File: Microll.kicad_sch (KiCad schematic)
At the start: 5 parts

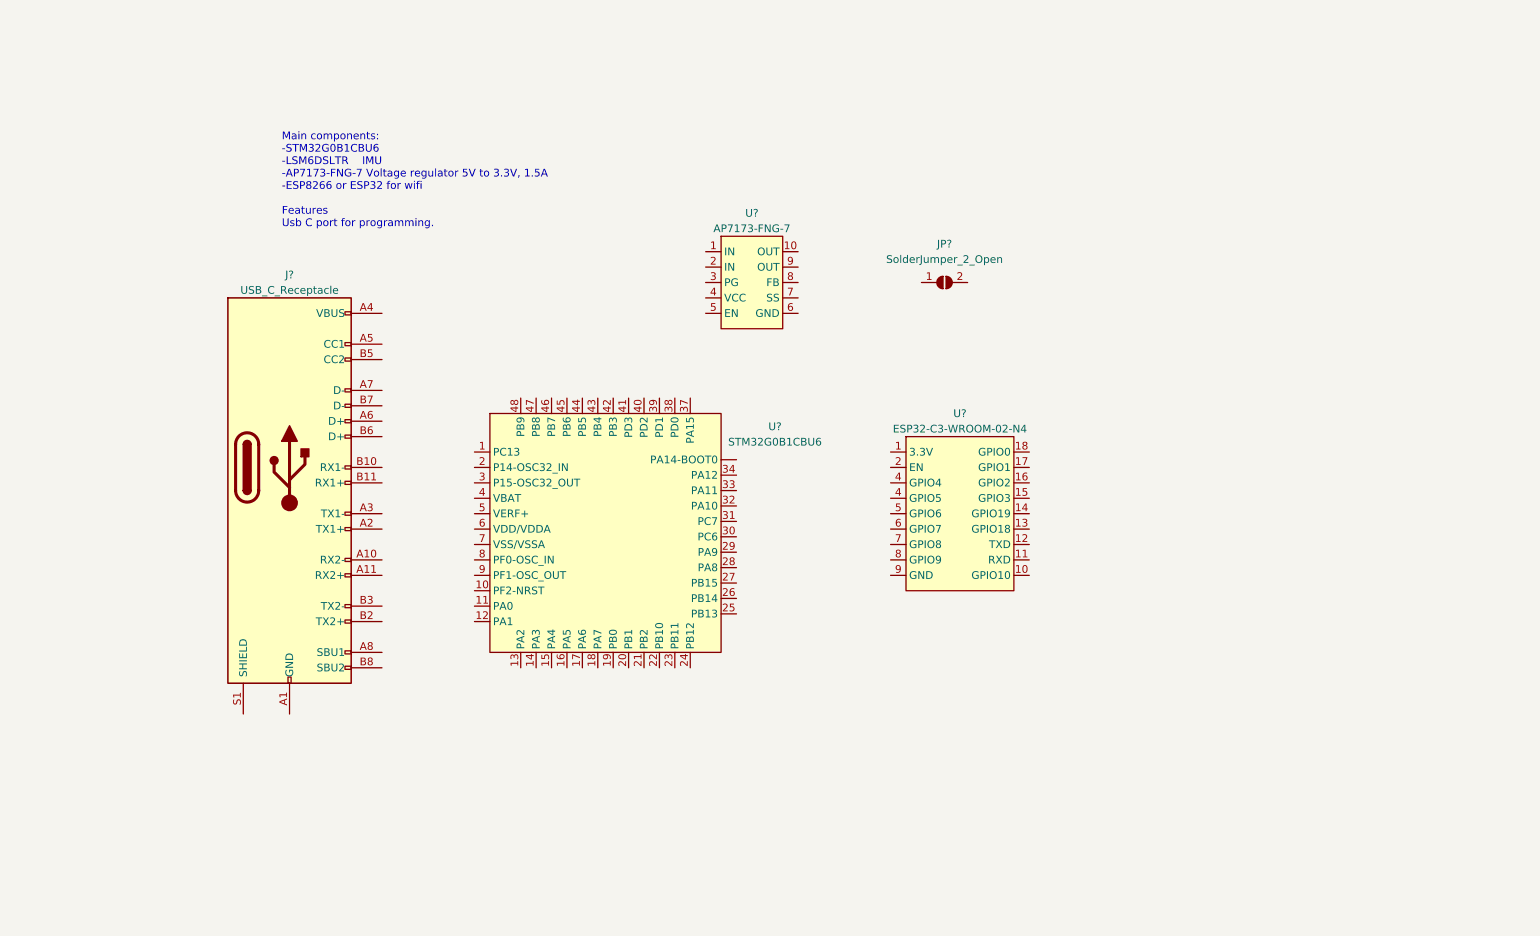
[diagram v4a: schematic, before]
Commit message: Added IMU. Initial placement of components on PCB to check spacing
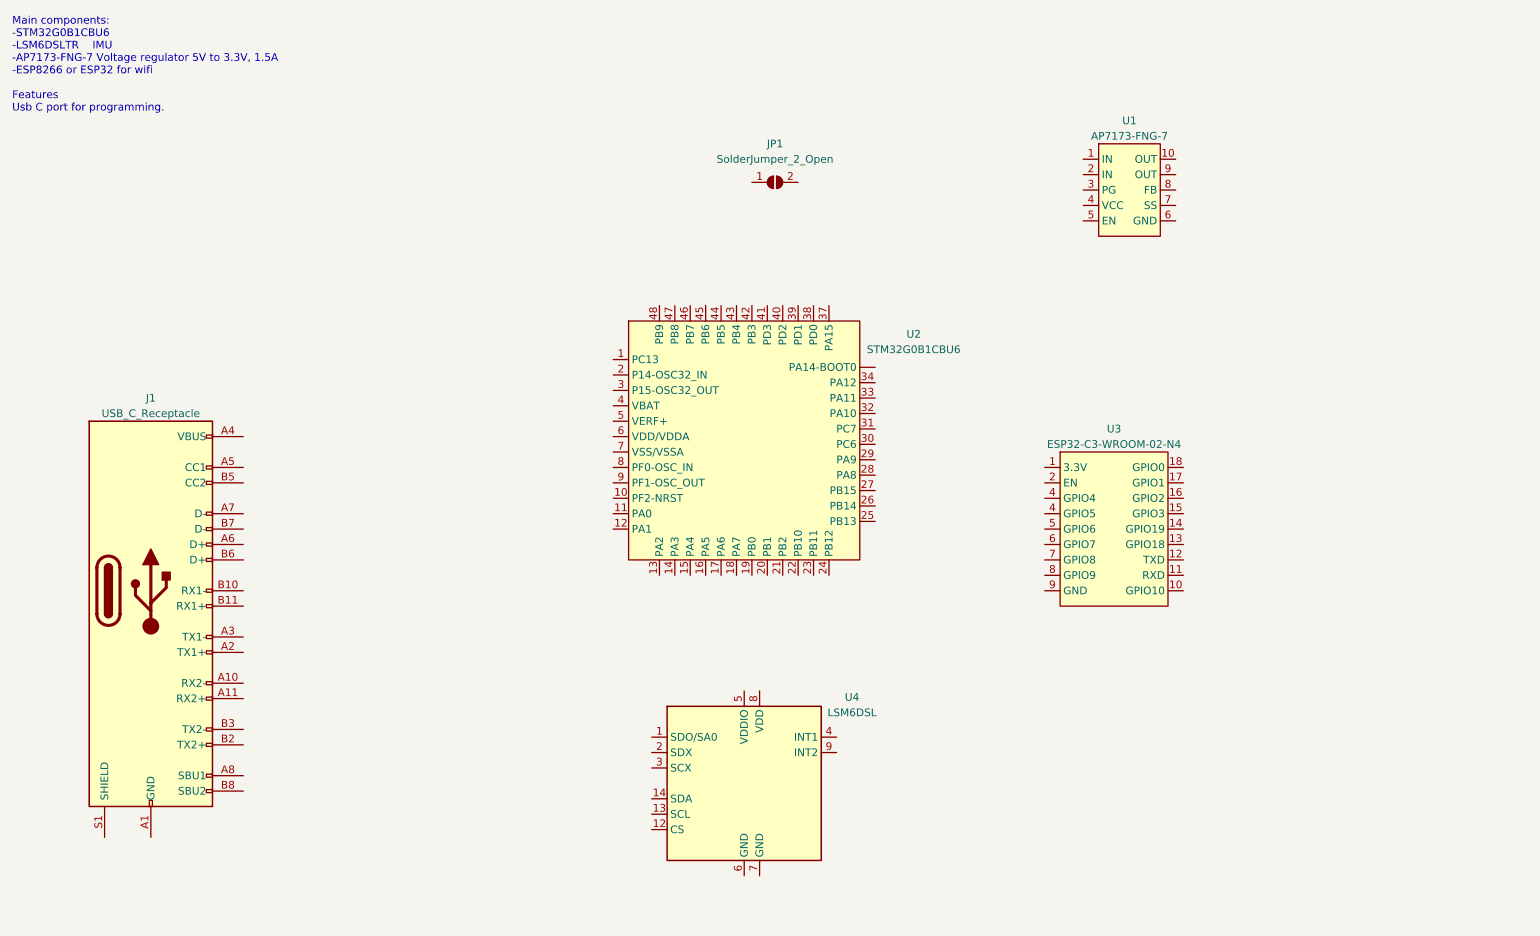
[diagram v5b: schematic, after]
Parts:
- added U4: LSM6DSL, Package_LGA:LGA-14_3x2.5mm_P0.5mm_LayoutBorder3x4y, symbol Sensor_Motion:LSM6DSL
- J1: renamed from J?; footprint (none) -> Connector_USB:USB_C_Receptacle_GCT_USB4105-xx-A_16P_TopMnt_Horizontal
- JP1: renamed from JP?; footprint (none) -> SolderJumper-2_P1.3mm_Open_RoundedPad1.0x1.5mm
- gave numbers to parts that had none: 3
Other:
- moved on the sheet: J1, JP1, U1, U2, U3
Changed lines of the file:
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@@
   (paper "A4")
   (text "Main components:\n-STM32G0B1CBU6	\n-LSM6DSLTR	IMU\n-AP7173-FNG-7 Voltage regulator 5V to 3.3V, 1.5A\n-ESP8266 or ESP32 for wifi\n\nFeatures\nUsb C port for programming."
-    (at 59.69 50.8 0)
+    (at 15.24 31.75 0)
     (effects (font (size 1.27 1.27)) (justify left bottom))
   )
-  (symbol (lib_id "Jumper:SolderJumper_2_Open") (at 168.91 59.69 0) (unit 1)
+  (symbol (lib_id "Jumper:SolderJumper_2_Open") (at 140.97 43.18 0) (unit 1)
     (in_bom yes) (on_board yes) (fields_autoplaced)
-    (property "Reference" "JP?" (id 0) (at 168.91 53.34 0))
-    (property "Value" "SolderJumper_2_Open" (id 1) (at 168.91 55.88 0))
-    (property "Footprint" "" (id 2) (at 168.91 59.69 0)
-      (effects (font (size 1.27 1.27)) hide)
-    )
-    (property "Datasheet" "~" (id 3) (at 168.91 59.69 0)
-      (effects (font (size 1.27 1.27)) hide)
-    )
-    (pin "1")
-    (pin "2")
-  )
-  (symbol (lib_id "ESP32:ESP32-C3-WROOM-02-N4") (at 171.45 93.98 0) (unit 1)
+    (property "Reference" "JP1" (id 0) (at 140.97 36.83 0))
+    (property "Value" "SolderJumper_2_Open" (id 1) (at 140.97 39.37 0))
+    (property "Footprint" "SolderJumper-2_P1.3mm_Open_RoundedPad1.0x1.5mm" (id 2) (at 140.97 43.18 0)
+      (effects (font (size 1.27 1.27)) hide)
+    )
+    (property "Datasheet" "~" (id 3) (at 140.97 43.18 0)
+      (effects (font (size 1.27 1.27)) hide)
+    )
+    (pin "1")
+    (pin "2")
+  )
+  (symbol (lib_id "ESP32:ESP32-C3-WROOM-02-N4") (at 196.85 96.52 0) (unit 1)
     (in_bom yes) (on_board yes)
-    (property "Reference" "U?" (id 0) (at 171.45 81.28 0))
-    (property "Value" "ESP32-C3-WROOM-02-N4" (id 1) (at 171.45 83.82 0))
-    (property "Footprint" "ESP32:ESP32-C3-WROOM-02-N4" (id 2) (at 171.45 93.98 0)
-      (effects (font (size 1.27 1.27)) hide)
-    )
-    (property "Datasheet" "" (id 3) (at 171.45 93.98 0)
+    (property "Reference" "U3" (id 0) (at 196.85 83.82 0))
+    (property "Value" "ESP32-C3-WROOM-02-N4" (id 1) (at 196.85 86.36 0))
+    (property "Footprint" "ESP32:ESP32-C3-WROOM-02-N4" (id 2) (at 196.85 96.52 0)
+      (effects (font (size 1.27 1.27)) hide)
+    )
+    (property "Datasheet" "" (id 3) (at 196.85 96.52 0)
       (effects (font (size 1.27 1.27)) hide)
     )
@@
     (pin "9")
   )
-  (symbol (lib_id "STM32:STM32G0B1CBU6") (at 113.03 101.6 0) (unit 1)
+  (symbol (lib_id "STM32:STM32G0B1CBU6") (at 135.89 86.36 0) (unit 1)
     (in_bom yes) (on_board yes) (fields_autoplaced)
-    (property "Reference" "U?" (id 0) (at 140.97 83.4388 0))
-    (property "Value" "STM32G0B1CBU6" (id 1) (at 140.97 85.9788 0))
-    (property "Footprint" "STM32:STM32G0B1CBU6" (id 2) (at 105.41 92.71 0)
-      (effects (font (size 1.27 1.27)) hide)
-    )
-    (property "Datasheet" "" (id 3) (at 105.41 92.71 0)
+    (property "Reference" "U2" (id 0) (at 163.83 68.1988 0))
+    (property "Value" "STM32G0B1CBU6" (id 1) (at 163.83 70.7388 0))
+    (property "Footprint" "STM32:STM32G0B1CBU6" (id 2) (at 128.27 77.47 0)
+      (effects (font (size 1.27 1.27)) hide)
+    )
+    (property "Datasheet" "" (id 3) (at 128.27 77.47 0)
       (effects (font (size 1.27 1.27)) hide)
     )
@@
     (pin "9")
   )
-  (symbol (lib_id "AP7173-FNG-7:AP7173-FNG-7") (at 137.16 57.15 0) (unit 1)
+  (symbol (lib_id "AP7173-FNG-7:AP7173-FNG-7") (at 199.39 41.91 0) (unit 1)
     (in_bom yes) (on_board yes)
-    (property "Reference" "U?" (id 0) (at 137.16 48.26 0))
-    (property "Value" "AP7173-FNG-7" (id 1) (at 137.16 50.8 0))
-    (property "Footprint" "AP7173-FNG-7:AP7173-FNG-7" (id 2) (at 135.89 57.15 0)
-      (effects (font (size 1.27 1.27)) hide)
-    )
-    (property "Datasheet" "" (id 3) (at 135.89 57.15 0)
+    (property "Reference" "U1" (id 0) (at 199.39 33.02 0))
+    (property "Value" "AP7173-FNG-7" (id 1) (at 199.39 35.56 0))
+    (property "Footprint" "AP7173-FNG-7:AP7173-FNG-7" (id 2) (at 198.12 41.91 0)
+      (effects (font (size 1.27 1.27)) hide)
+    )
+    (property "Datasheet" "" (id 3) (at 198.12 41.91 0)
       (effects (font (size 1.27 1.27)) hide)
     )
@@
     (pin "9")
   )
-  (symbol (lib_id "Connector:USB_C_Receptacle") (at 60.96 90.17 0) (unit 1)
+  (symbol (lib_id "Sensor_Motion:LSM6DSL") (at 135.89 142.24 0) (unit 1)
+    (in_bom yes) (on_board yes) (fields_autoplaced)
+    (property "Reference" "U4" (id 0) (at 153.67 128.0412 0))
+    (property "Value" "LSM6DSL" (id 1) (at 153.67 130.5812 0))
+    (property "Footprint" "Package_LGA:LGA-14_3x2.5mm_P0.5mm_LayoutBorder3x4y" (id 2) (at 125.73 160.02 0)
+      (effects (font (size 1.27 1.27)) (justify left) hide)
+    )
+    (property "Datasheet" "https://www.st.com/resource/en/datasheet/lsm6dsl.pdf" (id 3) (at 138.43 158.75 0)
+      (effects (font (size 1.27 1.27)) hide)
+    )
+    (pin "1")
+    (pin "10")
+    (pin "11")
+    (pin "12")
+    (pin "13")
+    (pin "14")
+    (pin "2")
+    (pin "3")
+    (pin "4")
+    (pin "5")
+    (pin "6")
+    (pin "7")
+    (pin "8")
+    (pin "9")
+  )
+  (symbol (lib_id "Connector:USB_C_Receptacle") (at 38.1 110.49 0) (unit 1)
     (in_bom yes) (on_board yes)
-    (property "Reference" "J?" (id 0) (at 60.96 58.42 0))
-    (property "Value" "USB_C_Receptacle" (id 1) (at 60.96 60.96 0))
-    (property "Footprint" "" (id 2) (at 64.77 90.17 0)
-      (effects (font (size 1.27 1.27)) hide)
-    )
-    (property "Datasheet" "https://www.usb.org/sites/default/files/documents/usb_type-c.zip" (id 3) (at 64.77 90.17 0)
+    (property "Reference" "J1" (id 0) (at 38.1 78.74 0))
+    (property "Value" "USB_C_Receptacle" (id 1) (at 38.1 81.28 0))
+    (property "Footprint" "Connector_USB:USB_C_Receptacle_GCT_USB4105-xx-A_16P_TopMnt_Horizontal" (id 2) (at 41.91 110.49 0)
+      (effects (font (size 1.27 1.27)) hide)
+    )
+    (property "Datasheet" "https://www.usb.org/sites/default/files/documents/usb_type-c.zip" (id 3) (at 41.91 110.49 0)
       (effects (font (size 1.27 1.27)) hide)
     )
@@
   (symbol_instances
     (path "/9dc9595c-915c-4807-bd39-25a9004629d5"
-      (reference "J?") (unit 1) (value "USB_C_Receptacle") (footprint "")
+      (reference "J1") (unit 1) (value "USB_C_Receptacle") (footprint "Connector_USB:USB_C_Receptacle_GCT_USB4105-xx-A_16P_TopMnt_Horizontal")
     )
     (path "/1c3b70c8-9878-40e4-8a0a-63d34ffadd04"
-      (reference "JP?") (unit 1) (value "SolderJumper_2_Open") (footprint "")
+      (reference "JP1") (unit 1) (value "SolderJumper_2_Open") (footprint "SolderJumper-2_P1.3mm_Open_RoundedPad1.0x1.5mm")
+    )
+    (path "/52ee2e49-a114-4de8-9329-acacfc8b62fc"
+      (reference "U1") (unit 1) (value "AP7173-FNG-7") (footprint "AP7173-FNG-7:AP7173-FNG-7")
+    )
+    (path "/5002f28f-3ca0-40e2-85f9-0c282d89806e"
+      (reference "U2") (unit 1) (value "STM32G0B1CBU6") (footprint "STM32:STM32G0B1CBU6")
     )
     (path "/3757d3b5-a25c-4772-93e2-fe7135fc4c50"
-      (reference "U?") (unit 1) (value "ESP32-C3-WROOM-02-N4") (footprint "ESP32:ESP32-C3-WROOM-02-N4")
-    )
-    (path "/5002f28f-3ca0-40e2-85f9-0c282d89806e"
-      (reference "U?") (unit 1) (value "STM32G0B1CBU6") (footprint "STM32:STM32G0B1CBU6")
-    )
-    (path "/52ee2e49-a114-4de8-9329-acacfc8b62fc"
-      (reference "U?") (unit 1) (value "AP7173-FNG-7") (footprint "AP7173-FNG-7:AP7173-FNG-7")
-    )
-  )
+      (reference "U3") (unit 1) (value "ESP32-C3-WROOM-02-N4") (footprint "ESP32:ESP32-C3-WROOM-02-N4")
+    )
+    (path "/82b316fb-a678-4a4b-9636-b2c35b750e09"
+      (reference "U4") (unit 1) (value "LSM6DSL") (footprint "Package_LGA:LGA-14_3x2.5mm_P0.5mm_LayoutBorder3x4y")
+    )
+  )
